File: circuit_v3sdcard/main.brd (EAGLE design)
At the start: 21.7 x 29.5 mm, 18 parts, among them CN1 SD, CN3 MICROSD, CN4 5035481020, IC1 C8051F381-GM, IC3 N25Q512A, IC4 KC2016K, IC6 MPU-9250

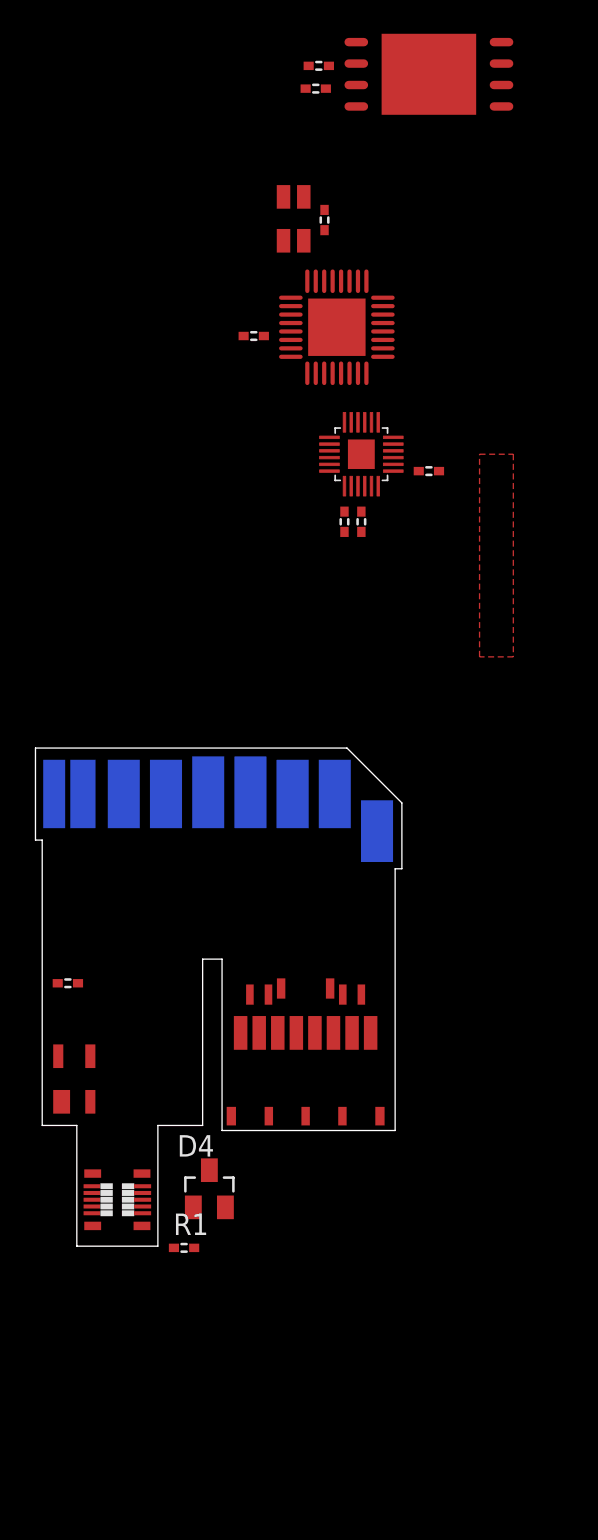
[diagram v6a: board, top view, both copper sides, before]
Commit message: Modified v3 circuit's parts position
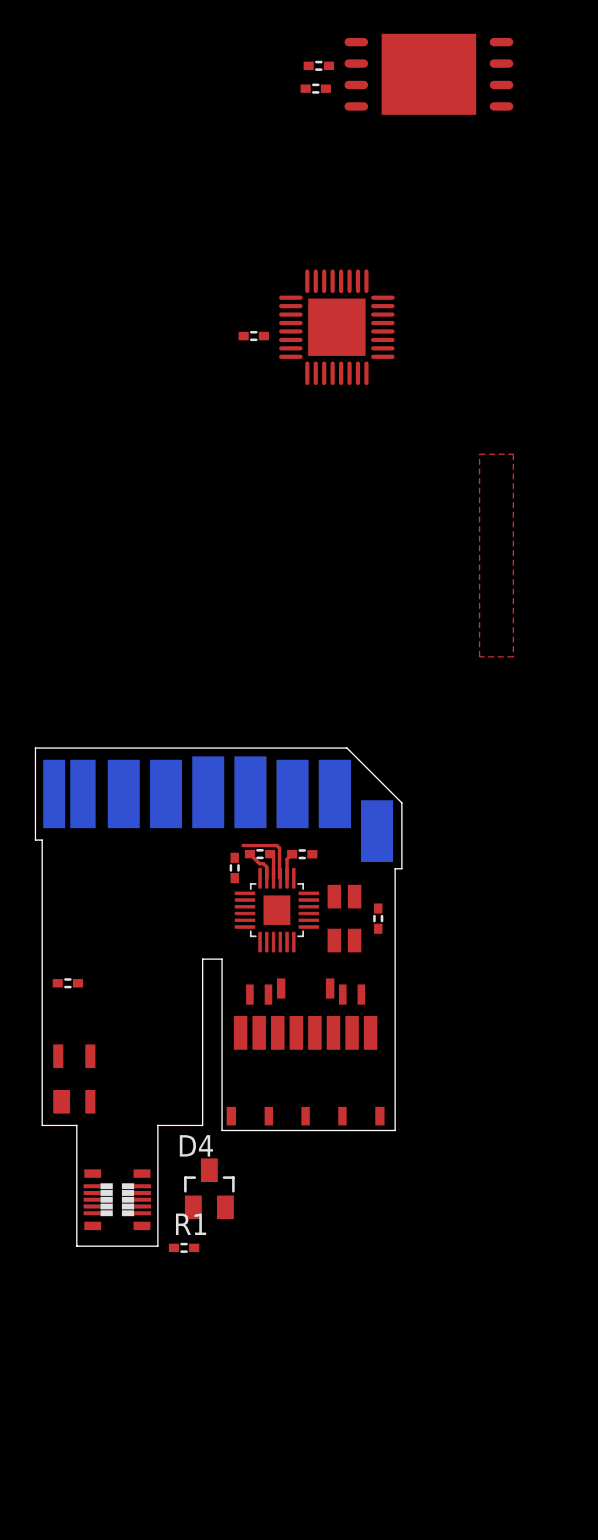
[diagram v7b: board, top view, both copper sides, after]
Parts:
- moved IC4 41.5 mm to (18.0, 19.5)
- moved C10 41.5 mm to (20.0, 19.5)
- moved IC6 27.5 mm to (14.0, 20.0), turned to 180 degrees
- moved C4 26.2 mm to (11.5, 22.5), turned to 270 degrees
- moved C3 20.6 mm to (13.0, 23.3), turned to 0 degrees
- moved C2 19.8 mm to (15.5, 23.3), turned to 180 degrees
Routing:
- net IMU_MISO: track 0.00 -> 4.03 mm
- net DGND: track 0.00 -> 1.98 mm
- net +3V3: track 0.00 -> 1.54 mm
- net N$13: track 0.00 -> 1.51 mm

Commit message: Modified flash memory position
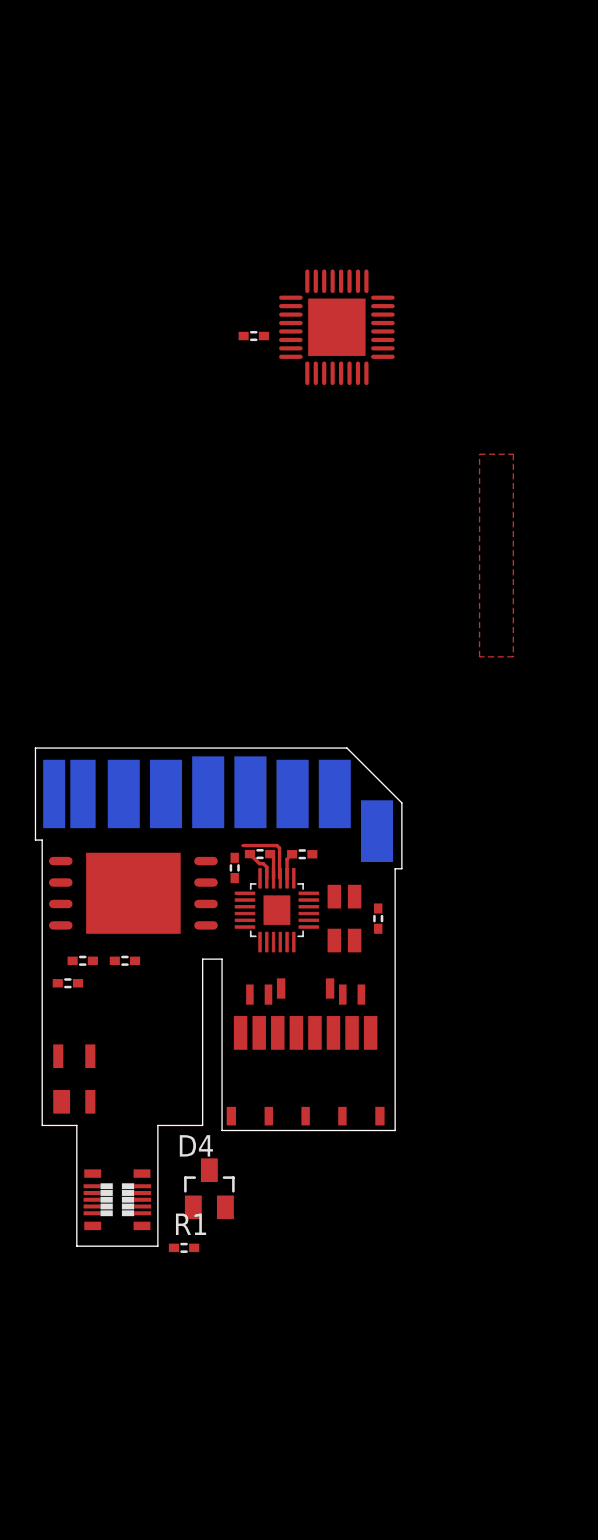
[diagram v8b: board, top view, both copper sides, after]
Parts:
- moved R26 54.2 mm to (5.00, 17.0)
- moved C9 53.5 mm to (2.50, 17.0), turned to 180 degrees
- moved IC3 51.6 mm to (5.50, 21.0)
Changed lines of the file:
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@@
 <attribute name="VALUE" x="13.2636" y="55.9051" size="1.27" layer="27" rot="R180"/>
 </element>
-<element name="IC3" library="EEPROM" package="V-PDFN-8" value="N25Q512A" x="23" y="69.5" smashed="yes" rot="R180">
-<attribute name="VALUE" x="26.635" y="73.5" size="0.8128" layer="27" rot="R180"/>
+<element name="IC3" library="EEPROM" package="V-PDFN-8" value="N25Q512A" x="5.5" y="21" smashed="yes" rot="R180">
+<attribute name="VALUE" x="9.135" y="25" size="0.8128" layer="27" rot="R180"/>
 </element>
-<element name="C9" library="reg,cap" package="1005" value="0.1u" x="16.3" y="68.65" smashed="yes">
-<attribute name="VALUE" x="15.665" y="66.745" size="1.27" layer="27"/>
+<element name="C9" library="reg,cap" package="1005" value="0.1u" x="2.5" y="17" smashed="yes" rot="R180">
+<attribute name="VALUE" x="3.135" y="18.905" size="1.27" layer="27" rot="R180"/>
 </element>
 <element name="IC4" library="Oscillator" package="KC2016K" value="KC2016K" x="18" y="19.5" smashed="yes" rot="R270">
@@
 <attribute name="VALUE" x="19.08" y="16.19" size="1.778" layer="27" rot="R180"/>
 </element>
-<element name="R26" library="reg,cap" package="1005" value="1k" x="16.48" y="70" smashed="yes">
-<attribute name="VALUE" x="15.845" y="68.095" size="1.27" layer="27"/>
+<element name="R26" library="reg,cap" package="1005" value="1k" x="5" y="17" smashed="yes">
+<attribute name="VALUE" x="4.365" y="15.095" size="1.27" layer="27"/>
 </element>
 <element name="D3" library="diode" package="SOT143" value="SP0503BAH" x="2" y="10" smashed="yes">
@@
 <wire x1="13.1905625" y1="22.754" x2="13.4" y2="22.5445625" width="0.2032" layer="1"/>
 <wire x1="13.4" y1="22.5445625" x2="13.4" y2="21.89" width="0.2032" layer="1"/>
-<wire x1="23" y1="69.5" x2="27.3" y2="71.405" width="0" layer="19" extent="1-1"/>
-<wire x1="15.88" y1="70" x2="23" y2="69.5" width="0" layer="19" extent="1-1"/>
-<wire x1="15.7" y1="68.65" x2="15.88" y2="70" width="0" layer="19" extent="1-1"/>
-<wire x1="14.825" y1="55.27" x2="15.7" y2="68.65" width="0" layer="19" extent="1-1"/>
+<wire x1="5.5" y1="21" x2="9.8" y2="22.905" width="0" layer="19" extent="1-1"/>
+<wire x1="4.4" y1="17" x2="5.5" y2="21" width="0" layer="19" extent="1-1"/>
+<wire x1="3.1" y1="17" x2="4.4" y2="17" width="0" layer="19" extent="1-1"/>
+<wire x1="14.825" y1="55.27" x2="3.1" y2="17" width="0" layer="19" extent="1-1"/>
 <wire x1="13.2286" y1="54" x2="14.825" y2="55.27" width="0" layer="19" extent="1-1"/>
 <wire x1="17.55" y1="54.52" x2="14.825" y2="55.27" width="0" layer="19" extent="1-1"/>
@@
 <wire x1="14.6" y1="21.89" x2="14.6" y2="23.01" width="0.2032" layer="1"/>
 <wire x1="14.6" y1="23.01" x2="14.9" y2="23.31" width="0.2032" layer="1"/>
-<wire x1="18.7" y1="68.865" x2="27.3" y2="70.135" width="0" layer="19" extent="1-1"/>
-<wire x1="18.7" y1="67.595" x2="18.7" y2="68.865" width="0" layer="19" extent="1-1"/>
-<wire x1="16.9" y1="68.65" x2="18.7" y2="68.865" width="0" layer="19" extent="1-1"/>
-<wire x1="14.825" y1="53.77" x2="18.7" y2="67.595" width="0" layer="19" extent="1-1"/>
+<wire x1="1.2" y1="20.365" x2="9.8" y2="21.635" width="0" layer="19" extent="1-1"/>
+<wire x1="1.2" y1="19.095" x2="1.2" y2="20.365" width="0" layer="19" extent="1-1"/>
+<wire x1="1.9" y1="17" x2="1.2" y2="20.365" width="0" layer="19" extent="1-1"/>
+<wire x1="14.825" y1="53.77" x2="1.2" y2="19.095" width="0" layer="19" extent="1-1"/>
 <wire x1="12.0286" y1="54" x2="14.825" y2="53.77" width="0" layer="19" extent="1-1"/>
 <wire x1="9.93" y1="26.98" x2="12.0286" y2="54" width="0" layer="19" extent="1-16"/>
@@
 <contactref element="IC3" pad="1"/>
 <contactref element="IC1" pad="27"/>
-<wire x1="18.3" y1="57.245" x2="27.3" y2="67.595" width="0" layer="19" extent="1-1"/>
+<wire x1="18.3" y1="57.245" x2="9.8" y2="19.095" width="0" layer="19" extent="1-1"/>
 </signal>
 <signal name="EEPROM_SCK">
@@
 <contactref element="IC1" pad="30"/>
 <contactref element="R26" pad="P$2"/>
-<wire x1="17.08" y1="70" x2="18.7" y2="70.135" width="0" layer="19" extent="1-1"/>
-<wire x1="16.8" y1="57.245" x2="17.08" y2="70" width="0" layer="19" extent="1-1"/>
+<wire x1="5.6" y1="17" x2="1.2" y2="21.635" width="0" layer="19" extent="1-1"/>
+<wire x1="16.8" y1="57.245" x2="5.6" y2="17" width="0" layer="19" extent="1-1"/>
 </signal>
 <signal name="EEPROM_MISO">
 <contactref element="IC3" pad="2"/>
 <contactref element="IC1" pad="28"/>
-<wire x1="17.8" y1="57.245" x2="27.3" y2="68.865" width="0" layer="19" extent="1-1"/>
+<wire x1="17.8" y1="57.245" x2="9.8" y2="20.365" width="0" layer="19" extent="1-1"/>
 </signal>
 <signal name="EEPROM_MOSI">
 <contactref element="IC3" pad="5"/>
 <contactref element="IC1" pad="29"/>
-<wire x1="17.3" y1="57.245" x2="18.7" y2="71.405" width="0" layer="19" extent="1-1"/>
+<wire x1="17.3" y1="57.245" x2="1.2" y2="22.905" width="0" layer="19" extent="1-1"/>
 </signal>
 <signal name="D-">
